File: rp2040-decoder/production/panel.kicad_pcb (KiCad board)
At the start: 4 copper layers, 70 x 70 mm, 535 parts, among them J4 5052702412, Q1 TPM2008, Q2 TPM2008, Q3 TPM2008, Q4 TPM2008, Q5 TPM2008, Q6 TPM2008, Q7 TPM2008, U1 W25Q64JVXGIQ, U2 AP63203WU, U3 RP2040, U4 MD9927, U5 MAX98357A, U6 LMV331, Y1 X252012MMB4SI

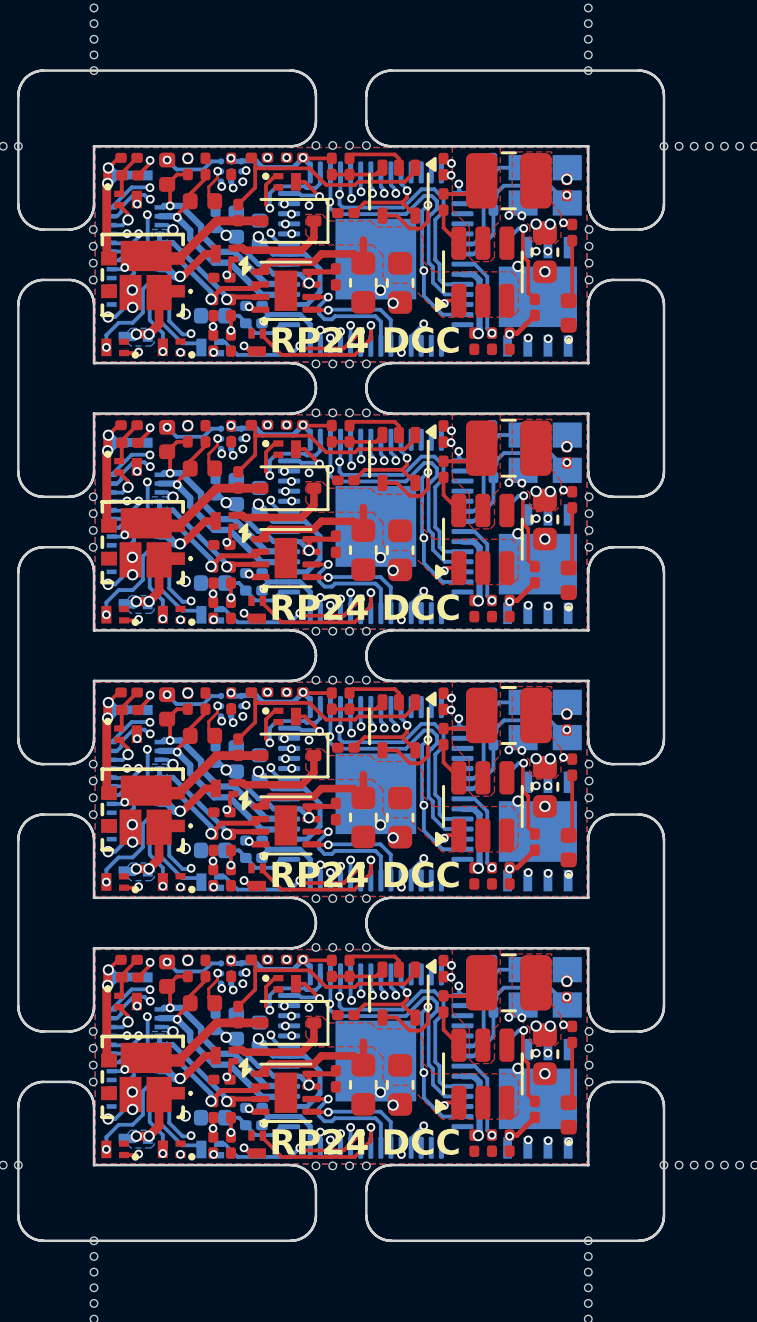
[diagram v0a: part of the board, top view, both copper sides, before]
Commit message: fix: allow cap to discharge below 8V rail voltage
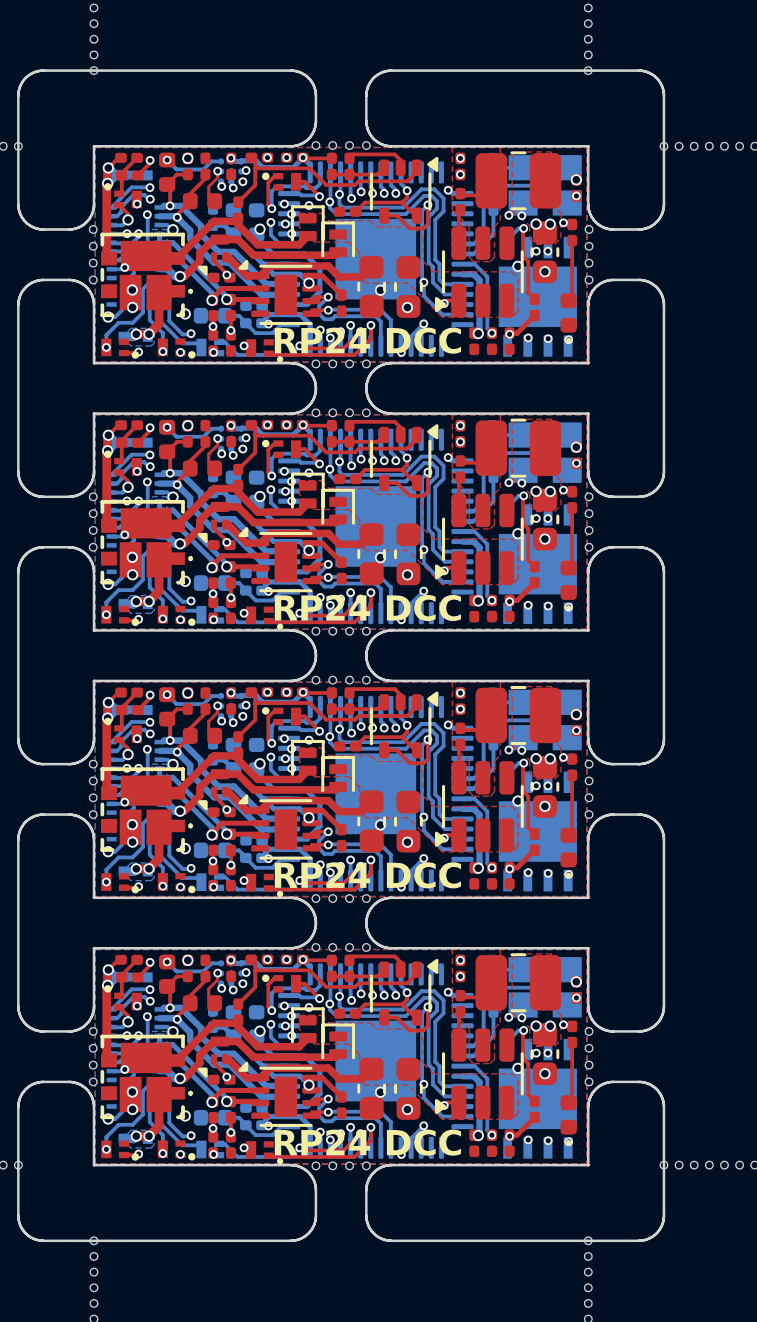
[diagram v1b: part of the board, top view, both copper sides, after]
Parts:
- removed the C10 at (144.3, 48.5)
- removed the C10 at (144.3, 59.1)
- removed the C10 at (144.3, 37.9)
- removed the C10 at (144.3, 69.7)
- removed the C12 at (143.5, 37.7)
- removed the C12 at (143.5, 58.9)
- removed the C12 at (143.5, 48.3)
- removed the C12 at (143.5, 69.5)
- removed the C17 at (152.6, 35.6)
- removed the C17 at (152.6, 46.2)
- removed the C17 at (152.6, 56.8)
- removed the C17 at (152.6, 67.4)
- removed the C18 at (149.4, 50.8)
- removed the C18 at (149.4, 40.2)
- removed the C18 at (149.4, 61.4)
- removed the C18 at (149.4, 72.0)
- removed the C19 at (148.3, 61.2)
- removed the C19 at (148.3, 71.8)
- removed the C19 at (148.3, 50.6)
- removed the C19 at (148.3, 40.0)
- removed the C3 at (157.4, 57.6)
- removed the C3 at (157.4, 36.4)
- removed the C3 at (157.4, 47.0)
- removed the C3 at (157.4, 68.2)
- removed the C4 at (150.8, 72.0)
- removed the C4 at (150.8, 50.8)
- removed the C4 at (150.8, 61.4)
- removed the C4 at (150.8, 40.2)
- removed the C5 at (148.7, 37.5)
- removed the C5 at (148.7, 58.6)
- removed the C5 at (148.7, 48.0)
- removed the C5 at (148.7, 69.2)
- removed the C6 at (152.6, 58.2)
- removed the C6 at (152.6, 47.6)
- removed the C6 at (152.6, 68.8)
- removed the C6 at (152.6, 37.0)
- removed the C8 at (145.3, 38.2)
- removed the C8 at (145.3, 70.0)
- removed the C8 at (145.3, 48.8)
- removed the C8 at (145.3, 59.4)
- removed the D4 at (146.4, 69.6)
- removed the D4 at (146.4, 48.4)
- removed the D4 at (146.4, 59.0)
- removed the D4 at (146.4, 37.8)
- removed the L1 at (155.2, 46.8)
- removed the L1 at (155.2, 68.0)
- removed the L1 at (155.2, 36.2)
- removed the L1 at (155.2, 57.4)
- removed the Q2 at (145.2, 63.8)
- removed the Q2 at (145.2, 53.2)
- removed the Q2 at (145.2, 74.4)
- removed the Q2 at (145.2, 42.6)
- removed the Q7 at (143.9, 49.7)
- removed the Q7 at (143.9, 70.9)
- removed the Q7 at (143.9, 60.3)
- removed the Q7 at (143.9, 39.1)
- removed the R3 at (144.4, 58.6)
- removed the R3 at (144.4, 69.2)
- removed the R3 at (144.4, 48.0)
- removed the R3 at (144.4, 37.4)
- removed the U4 at (146.3, 51.1)
- removed the U4 at (146.3, 72.3)
- removed the U4 at (146.3, 40.5)
- removed the U4 at (146.3, 61.7)
- removed the U6 at (150.8, 57.8)
- removed the U6 at (150.8, 68.4)
- removed the U6 at (150.8, 36.6)
- removed the U6 at (150.8, 47.2)
- added C10: 10uF, Capacitor_SMD:C_0402_1005Metric, B.Cu at (144.2, 37.8)
- added C10: 10uF, Capacitor_SMD:C_0402_1005Metric, B.Cu at (144.2, 59.0)
- added C10: 10uF, Capacitor_SMD:C_0402_1005Metric, B.Cu at (144.2, 48.4)
- added C10: 10uF, Capacitor_SMD:C_0402_1005Metric, B.Cu at (144.2, 69.6)
- added C12: 100nF, Capacitor_SMD:C_0201_0603Metric, B.Cu at (143.4, 37.6)
- added C12: 100nF, Capacitor_SMD:C_0201_0603Metric, B.Cu at (143.4, 48.2)
- added C12: 100nF, Capacitor_SMD:C_0201_0603Metric, B.Cu at (143.4, 58.8)
- added C12: 100nF, Capacitor_SMD:C_0201_0603Metric, B.Cu at (143.4, 69.4)
- added C17: 100nF, Capacitor_SMD:C_0201_0603Metric, F.Cu at (153.2, 35.6)
- added C17: 100nF, Capacitor_SMD:C_0201_0603Metric, F.Cu at (153.2, 67.4)
- added C17: 100nF, Capacitor_SMD:C_0201_0603Metric, F.Cu at (153.2, 56.8)
- added C17: 100nF, Capacitor_SMD:C_0201_0603Metric, F.Cu at (153.2, 46.2)
- added C18: 10uF, Capacitor_SMD:C_0603_1608Metric, F.Cu at (149.7, 72.2)
- added C18: 10uF, Capacitor_SMD:C_0603_1608Metric, F.Cu at (149.7, 51.0)
- added C18: 10uF, Capacitor_SMD:C_0603_1608Metric, F.Cu at (149.7, 61.6)
- added C18: 10uF, Capacitor_SMD:C_0603_1608Metric, F.Cu at (149.7, 40.4)
- added C19: 100nF, Capacitor_SMD:C_0201_0603Metric, F.Cu at (148.5, 41.0)
- added C19: 100nF, Capacitor_SMD:C_0201_0603Metric, F.Cu at (148.5, 72.8)
- added C19: 100nF, Capacitor_SMD:C_0201_0603Metric, F.Cu at (148.5, 51.6)
- added C19: 100nF, Capacitor_SMD:C_0201_0603Metric, F.Cu at (148.5, 62.2)
- added C3: 10pF, Capacitor_SMD:C_0201_0603Metric, F.Cu at (157.8, 68.2)
- added C3: 10pF, Capacitor_SMD:C_0201_0603Metric, F.Cu at (157.8, 57.6)
- added C3: 10pF, Capacitor_SMD:C_0201_0603Metric, F.Cu at (157.8, 36.5)
- added C3: 10pF, Capacitor_SMD:C_0201_0603Metric, F.Cu at (157.8, 47.0)
- added C4: 10uF, Capacitor_SMD:C_0603_1608Metric, F.Cu at (151.2, 72.2)
- added C4: 10uF, Capacitor_SMD:C_0603_1608Metric, F.Cu at (151.2, 40.4)
- added C4: 10uF, Capacitor_SMD:C_0603_1608Metric, F.Cu at (151.2, 61.6)
- added C4: 10uF, Capacitor_SMD:C_0603_1608Metric, F.Cu at (151.2, 51.0)
- added C5: 100nF, Capacitor_SMD:C_0201_0603Metric, F.Cu at (148.8, 37.4)
- added C5: 100nF, Capacitor_SMD:C_0201_0603Metric, F.Cu at (148.8, 48.0)
- added C5: 100nF, Capacitor_SMD:C_0201_0603Metric, F.Cu at (148.8, 69.2)
- added C5: 100nF, Capacitor_SMD:C_0201_0603Metric, F.Cu at (148.8, 58.6)
- added C6: 100nF, Capacitor_SMD:C_0201_0603Metric, F.Cu at (153.2, 47.6)
- added C6: 100nF, Capacitor_SMD:C_0201_0603Metric, F.Cu at (153.2, 58.2)
- added C6: 100nF, Capacitor_SMD:C_0201_0603Metric, F.Cu at (153.2, 68.8)
- added C6: 100nF, Capacitor_SMD:C_0201_0603Metric, F.Cu at (153.2, 37.0)
- added C8: 10uF, Capacitor_SMD:C_0402_1005Metric, B.Cu at (145.2, 48.4)
- added C8: 10uF, Capacitor_SMD:C_0402_1005Metric, B.Cu at (145.2, 59.0)
- added C8: 10uF, Capacitor_SMD:C_0402_1005Metric, B.Cu at (145.2, 37.8)
- added C8: 10uF, Capacitor_SMD:C_0402_1005Metric, B.Cu at (145.2, 69.6)
- added D3: PSBD2FD40V1H, Diode_SMD:D_SOD-882, F.Cu at (148.4, 49.2)
- added D3: PSBD2FD40V1H, Diode_SMD:D_SOD-882, F.Cu at (148.4, 70.5)
- added D3: PSBD2FD40V1H, Diode_SMD:D_SOD-882, F.Cu at (148.4, 59.9)
- added D3: PSBD2FD40V1H, Diode_SMD:D_SOD-882, F.Cu at (148.4, 38.6)
- added D4: PSBD2FD40V1H, Diode_SMD:D_SOD-882, F.Cu at (147.2, 48.6)
- added D4: PSBD2FD40V1H, Diode_SMD:D_SOD-882, F.Cu at (147.2, 69.8)
- added D4: PSBD2FD40V1H, Diode_SMD:D_SOD-882, F.Cu at (147.2, 59.2)
- added D4: PSBD2FD40V1H, Diode_SMD:D_SOD-882, F.Cu at (147.2, 38.0)
- added L1: 4.7uH, Inductor_SMD:L_1008_2520Metric, F.Cu at (155.5, 57.4)
- added L1: 4.7uH, Inductor_SMD:L_1008_2520Metric, F.Cu at (155.5, 46.8)
- added L1: 4.7uH, Inductor_SMD:L_1008_2520Metric, F.Cu at (155.5, 68.0)
- added L1: 4.7uH, Inductor_SMD:L_1008_2520Metric, F.Cu at (155.5, 36.2)
- added Q2: TPM2008, Local Library:Diodes_DFN1006-3, F.Cu at (145.3, 74.6)
- added Q2: TPM2008, Local Library:Diodes_DFN1006-3, F.Cu at (145.3, 42.8)
- added Q2: TPM2008, Local Library:Diodes_DFN1006-3, F.Cu at (145.3, 64.0)
- added Q2: TPM2008, Local Library:Diodes_DFN1006-3, F.Cu at (145.3, 53.4)
- added Q7: TPM2008, Local Library:Diodes_DFN1006-3, F.Cu at (143.7, 38.9)
- added Q7: TPM2008, Local Library:Diodes_DFN1006-3, F.Cu at (143.7, 49.5)
- added Q7: TPM2008, Local Library:Diodes_DFN1006-3, F.Cu at (143.7, 70.7)
- added Q7: TPM2008, Local Library:Diodes_DFN1006-3, F.Cu at (143.7, 60.0)
- added R3: 100K, Resistor_SMD:R_0201_0603Metric, F.Cu at (144.4, 37.3)
- added R3: 100K, Resistor_SMD:R_0201_0603Metric, F.Cu at (144.4, 69.1)
- added R3: 100K, Resistor_SMD:R_0201_0603Metric, F.Cu at (144.4, 47.9)
- added R3: 100K, Resistor_SMD:R_0201_0603Metric, F.Cu at (144.4, 58.5)
- added U4: MD9927, Package_DFN_QFN:DFN-8-1EP_2x2mm_P0.5mm_EP0.9x1.6mm, F.Cu at (146.3, 72.5)
- added U4: MD9927, Package_DFN_QFN:DFN-8-1EP_2x2mm_P0.5mm_EP0.9x1.6mm, F.Cu at (146.3, 61.9)
- added U4: MD9927, Package_DFN_QFN:DFN-8-1EP_2x2mm_P0.5mm_EP0.9x1.6mm, F.Cu at (146.3, 40.7)
- added U4: MD9927, Package_DFN_QFN:DFN-8-1EP_2x2mm_P0.5mm_EP0.9x1.6mm, F.Cu at (146.3, 51.3)
- added U6: LMV331, Package_TO_SOT_SMD:SOT-353_SC-70-5, F.Cu at (150.9, 68.4)
- added U6: LMV331, Package_TO_SOT_SMD:SOT-353_SC-70-5, F.Cu at (150.9, 57.8)
- added U6: LMV331, Package_TO_SOT_SMD:SOT-353_SC-70-5, F.Cu at (150.9, 47.2)
- added U6: LMV331, Package_TO_SOT_SMD:SOT-353_SC-70-5, F.Cu at (150.9, 36.6)
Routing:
- net Board_3-/CAP+: track 2.72 -> 8.30 mm
- net Board_2-/CAP+: track 2.72 -> 8.30 mm
- net Board_1-/CAP+: track 2.72 -> 8.30 mm
- net Board_0-/CAP+: track 2.72 -> 8.30 mm
- net Board_1-/CAP_VDC: track 9.55 -> 6.60 mm
- net Board_0-/CAP_VDC: track 9.55 -> 6.60 mm
- net Board_2-/CAP_VDC: track 9.55 -> 6.60 mm
- net Board_3-/CAP_VDC: track 9.55 -> 6.60 mm
- net Board_3-VDC: track 4.41 -> 7.10 mm
- net Board_2-VDC: track 4.41 -> 7.10 mm
- net Board_1-VDC: track 4.41 -> 7.10 mm
- net Board_0-VDC: track 4.41 -> 7.10 mm
- net Board_2-+3.3V: track 42.6 -> 43.8 mm, vias 14 -> 13
- net Board_0-+3.3V: track 42.6 -> 43.8 mm, vias 14 -> 13
- net Board_1-+3.3V: track 42.6 -> 43.8 mm, vias 14 -> 13
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
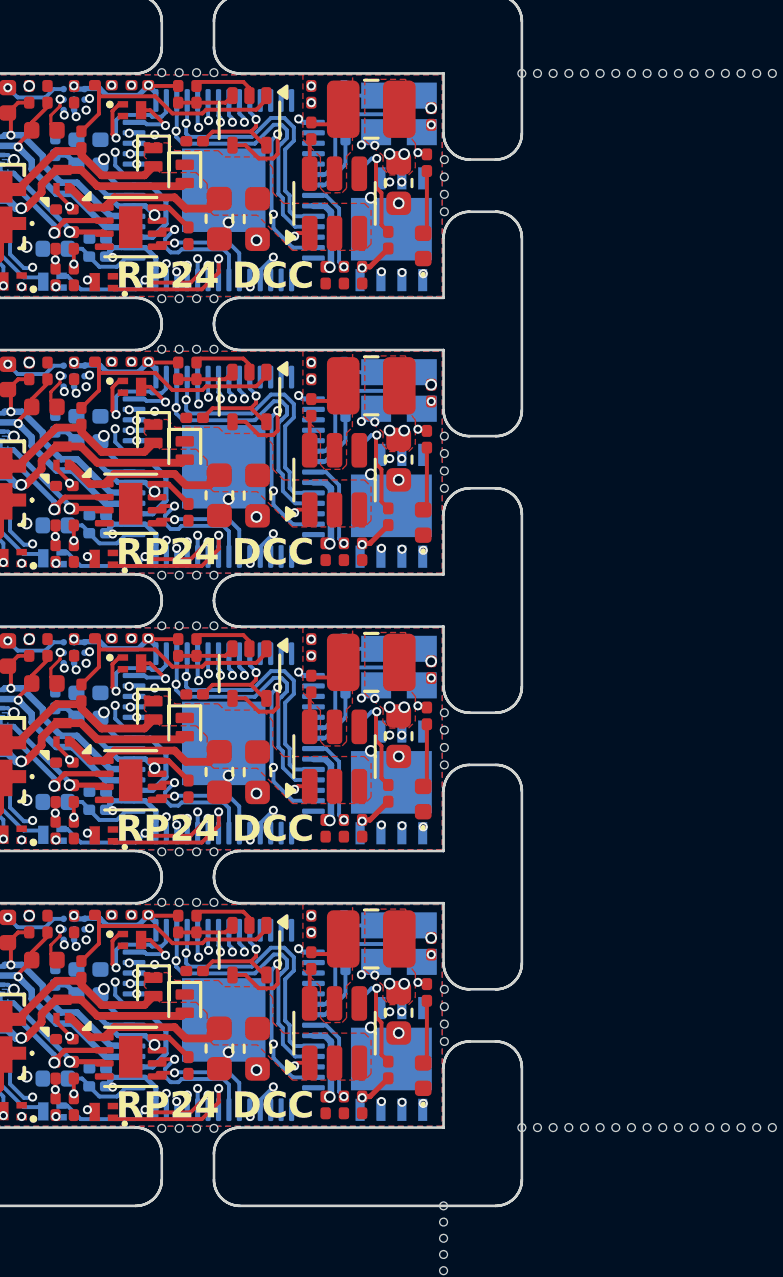
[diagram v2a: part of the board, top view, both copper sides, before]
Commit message: fix: update footprints and component rotations
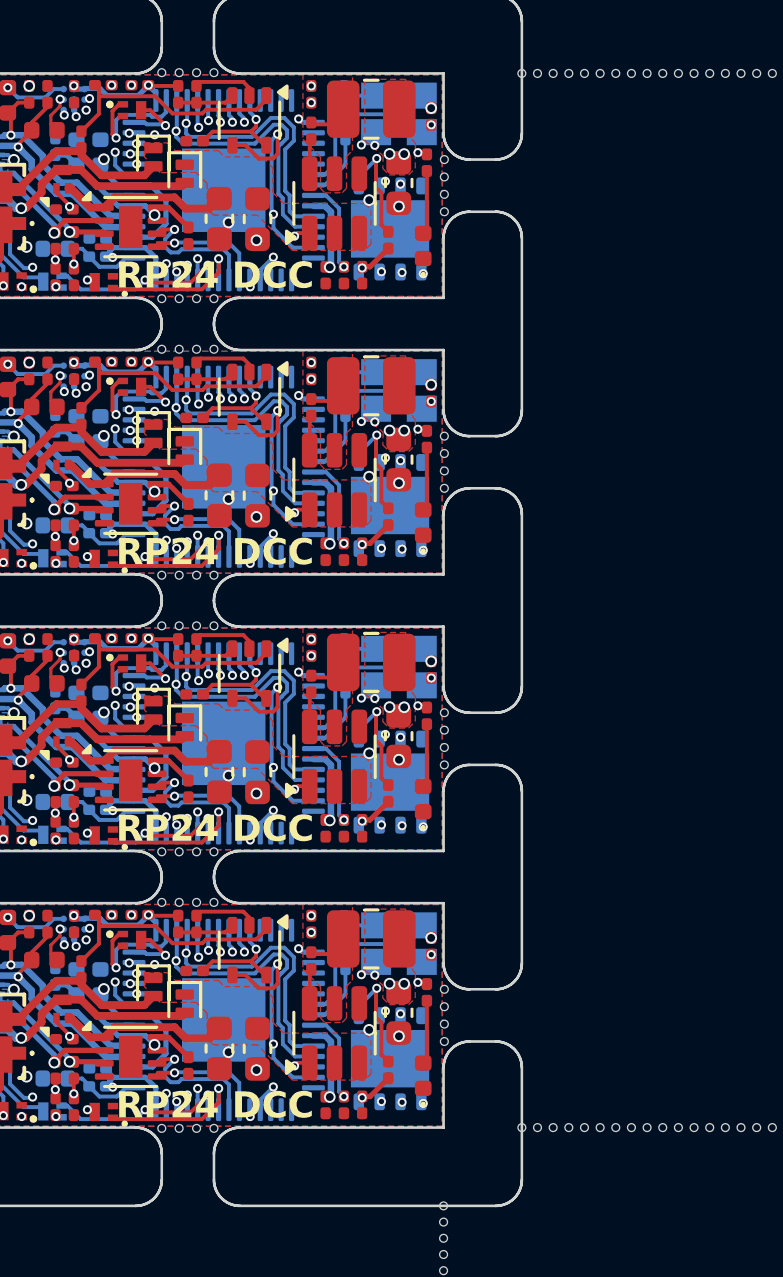
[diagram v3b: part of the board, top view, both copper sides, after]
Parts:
- removed the U1 at (156.3, 51.4)
- removed the U1 at (156.3, 72.6)
- removed the U1 at (156.3, 40.8)
- removed the U1 at (156.3, 62.0)
- added U1: W25Q64JVXGIQ, Package_SON:WSON-8-1EP_4x4mm_P0.8mm_EP2.2x3mm, B.Cu at (156.2, 51.4)
- added U1: W25Q64JVXGIQ, Package_SON:WSON-8-1EP_4x4mm_P0.8mm_EP2.2x3mm, B.Cu at (156.2, 62.0)
- added U1: W25Q64JVXGIQ, Package_SON:WSON-8-1EP_4x4mm_P0.8mm_EP2.2x3mm, B.Cu at (156.2, 72.6)
- added U1: W25Q64JVXGIQ, Package_SON:WSON-8-1EP_4x4mm_P0.8mm_EP2.2x3mm, B.Cu at (156.2, 40.8)
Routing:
- net Board_1-/BOOT: track 15.1 -> 15.6 mm
- net Board_0-/BOOT: track 15.1 -> 15.6 mm
- net Board_3-/BOOT: track 15.1 -> 15.6 mm
- net Board_2-/BOOT: track 15.1 -> 15.6 mm
